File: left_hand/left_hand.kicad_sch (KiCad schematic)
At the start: 11 parts, among them M1 Motor_Servo, M2 Motor_Servo, M3 Motor_Servo, M4 Motor_Servo, M5 Motor_Servo, Q1 Q_NMOS_GDS, U1 MCP23017_SP, U2 PCA9615DP, U3 PCA9685PW

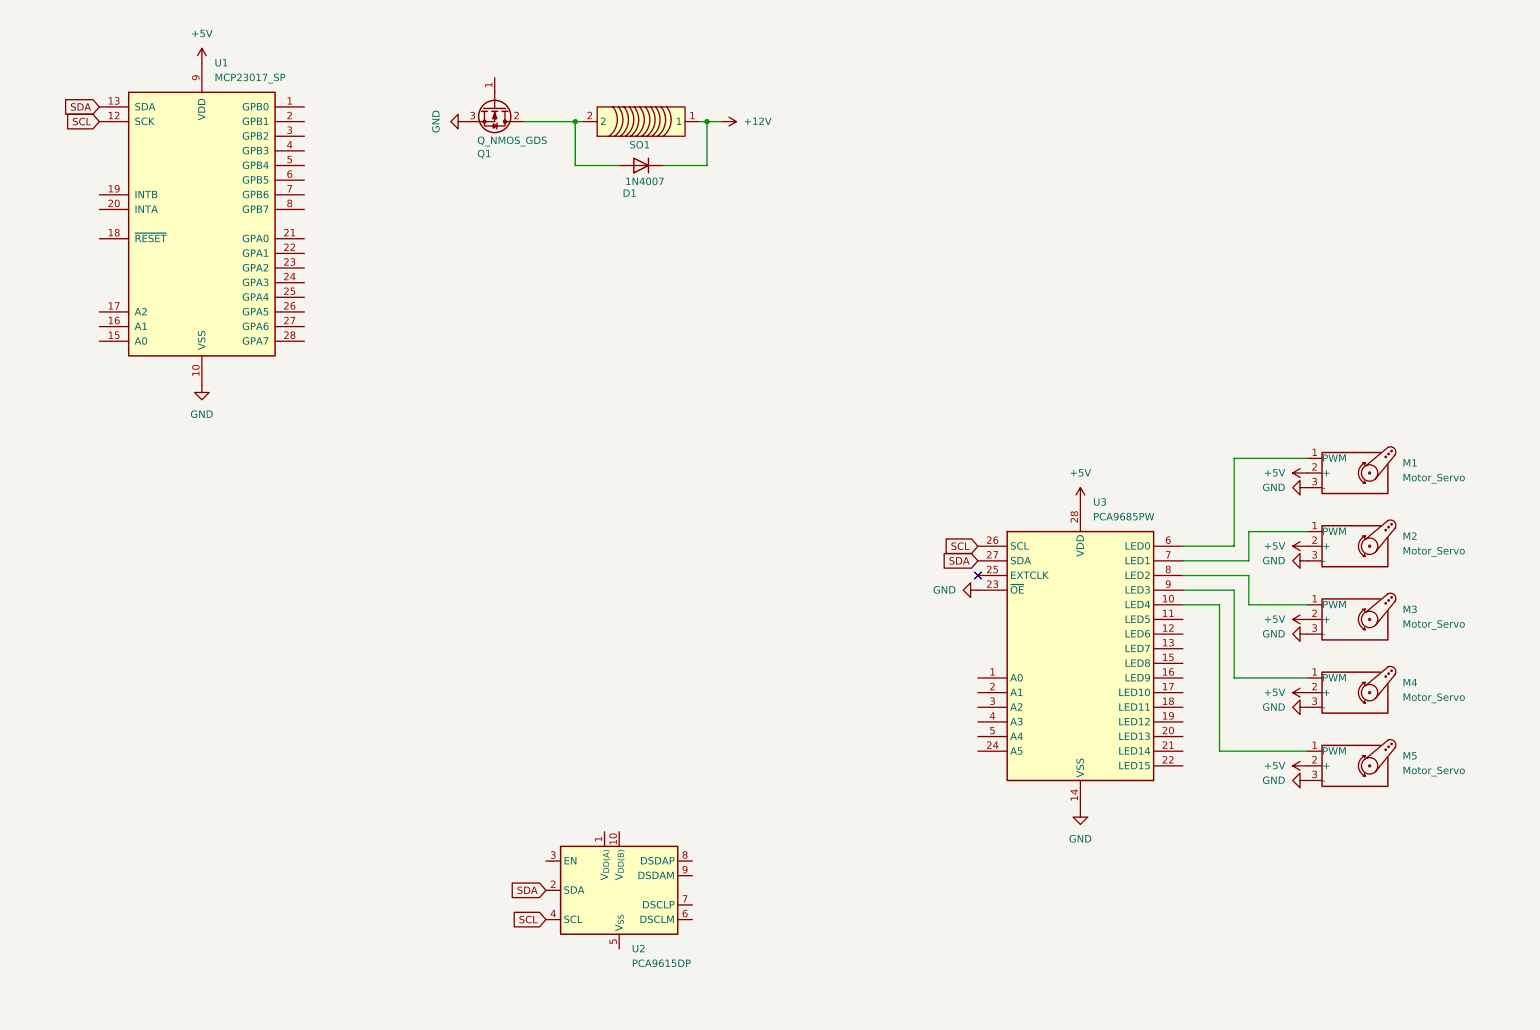
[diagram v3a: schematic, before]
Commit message: I2C diff. and single side bus changes
Added differential termination on each end. Todo: determine maximum differential bias voltage. Added pull up resistors for I2C lines.

Added decoupling caps.
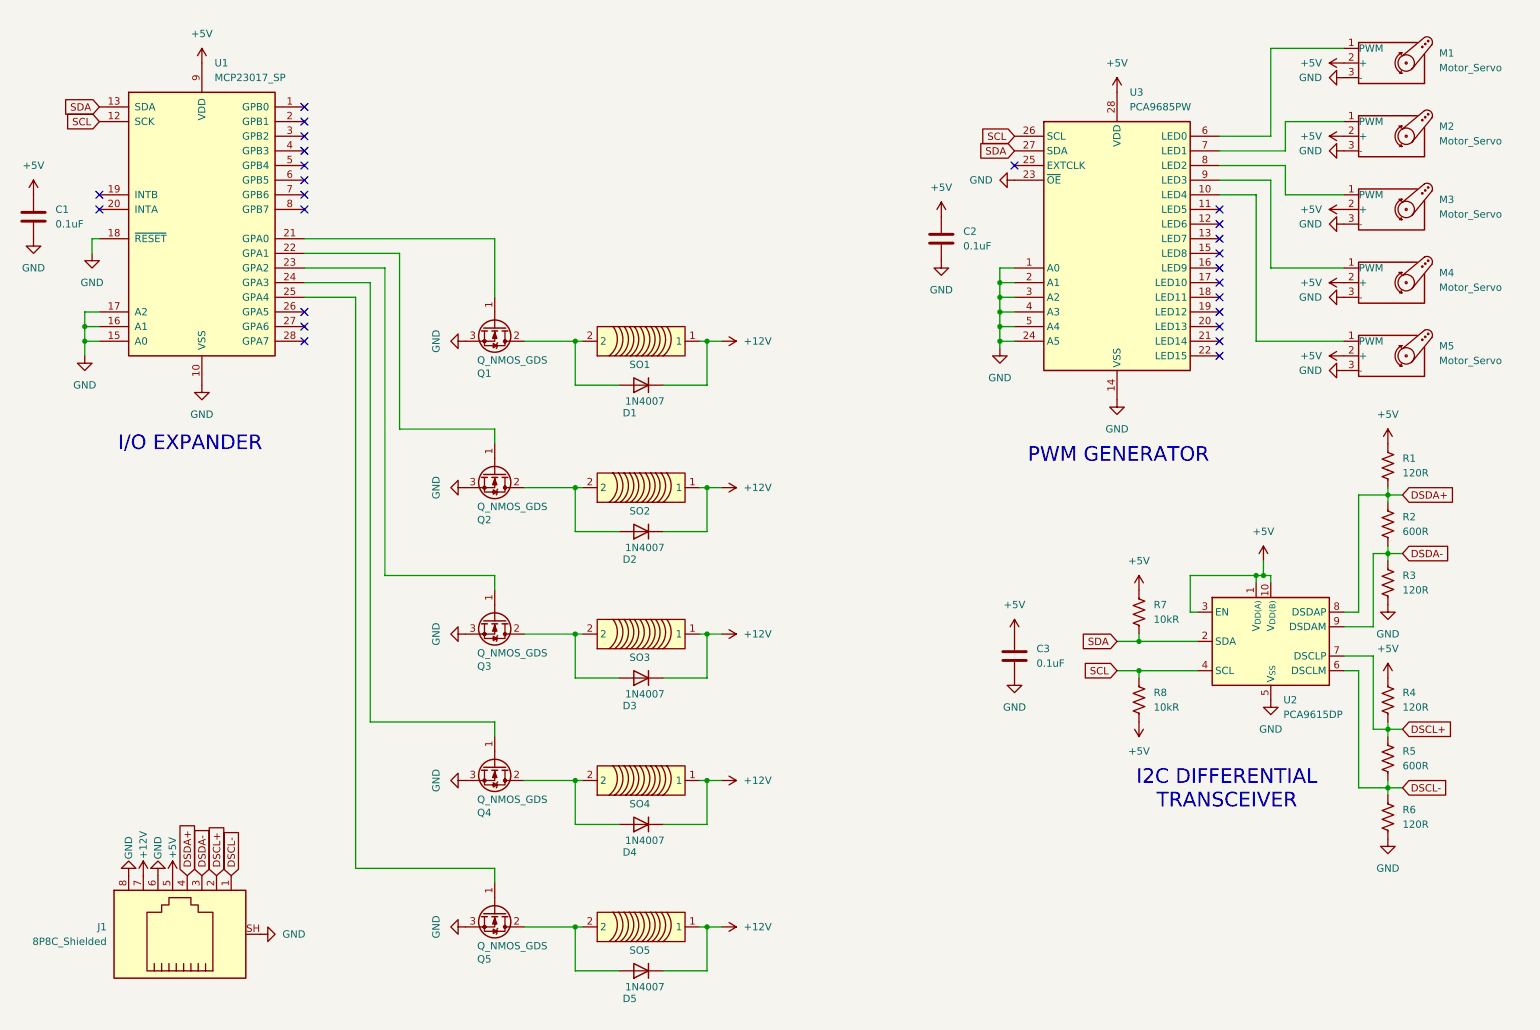
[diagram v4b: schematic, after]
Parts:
- added C1, C2, C3: 0.1uF, Capacitor_THT:C_Disc_D8.0mm_W2.5mm_P5.00mm, symbol Device:C
- added D2, D3, D4, D5: 1N4007, Diode_THT:D_DO-41_SOD81_P10.16mm_Horizontal, symbol Diode:1N4007
- added J1: 8P8C_Shielded, Connector_RJ:RJ45_Amphenol_RJHSE5380, symbol Connector:8P8C_Shielded
- added Q2, Q3, Q4, Q5: Q_NMOS_GDS, Package_TO_SOT_THT:TO-220-3_Vertical, symbol Device:Q_NMOS_GDS
- added R1, R3, R4, R6: 120R, symbol Device:R_US
- added R2, R5: 600R, symbol Device:R_US
- added R7, R8: 10kR, symbol Device:R_US
- added SO2, SO3, SO4, SO5: ~, symbol bh_symbol_library:SOLENOID
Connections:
- net +12V: now also D2.1 (K), D3.1 (K), D4.1 (K), D5.1 (K), J1.7, SO2.1, SO3.1, SO4.1, SO5.1
- net +5V: now also U2.1 (V_{DD(A)}), U2.10 (V_{DD(B)}), U2.3 (EN), C1.1, C2.1, C3.1, J1.5, R1.1, R4.1, R7.1, R8.2
- net GND: now also U1.15 (A0), U1.16 (A1), U1.17 (A2), U1.18 (~{RESET}), U2.5 (V_{SS}), U3.1 (A0), U3.2 (A1), U3.24 (A5), U3.3 (A2), U3.4 (A3), U3.5 (A4), C1.2, C2.2, C3.2, J1.6, J1.8, J1.SH, Q2.3 (S), Q3.3 (S), Q4.3 (S), Q5.3 (S), R3.2, R6.2
- net SCL: now also R8.1
- net SDA: now also R7.2
- net at U1.21 (GPA0): now also Q1.1 (G)
- net at U1.22 (GPA1): now also Q2.1 (G)
- net at U1.23 (GPA2): now also Q3.1 (G)
- net at U1.24 (GPA3): now also Q4.1 (G)
- net at U1.25 (GPA4): now also Q5.1 (G)
- net DSCL-: now reaches U2.6 (DSCLM)
- net DSCL-: now also J1.1, R5.2, R6.1
- net DSCL+: now reaches U2.7 (DSCLP)
- net DSCL+: now also J1.2, R4.2, R5.1
- net DSDA+: now reaches U2.8 (DSDAP)
- net DSDA+: now also J1.4, R1.2, R2.1
- net DSDA-: now reaches U2.9 (DSDAM)
- net DSDA-: now also J1.3, R2.2, R3.1
- new net: D4.2 (A), Q4.2 (D), SO4.2
- new net: D3.2 (A), Q3.2 (D), SO3.2
- new net: D5.2 (A), Q5.2 (D), SO5.2
- new net: D2.2 (A), Q2.2 (D), SO2.2
- no-connect marks 1 -> 25
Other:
- note added: "I/O EXPANDER"
- note added: "I2C DIFFERENTIAL TRANSCEIVER"
- note added: "PWM GENERATOR"
- moved on the sheet: D1, M1, M2, M3, M4, M5, Q1, SO1, U2, U3

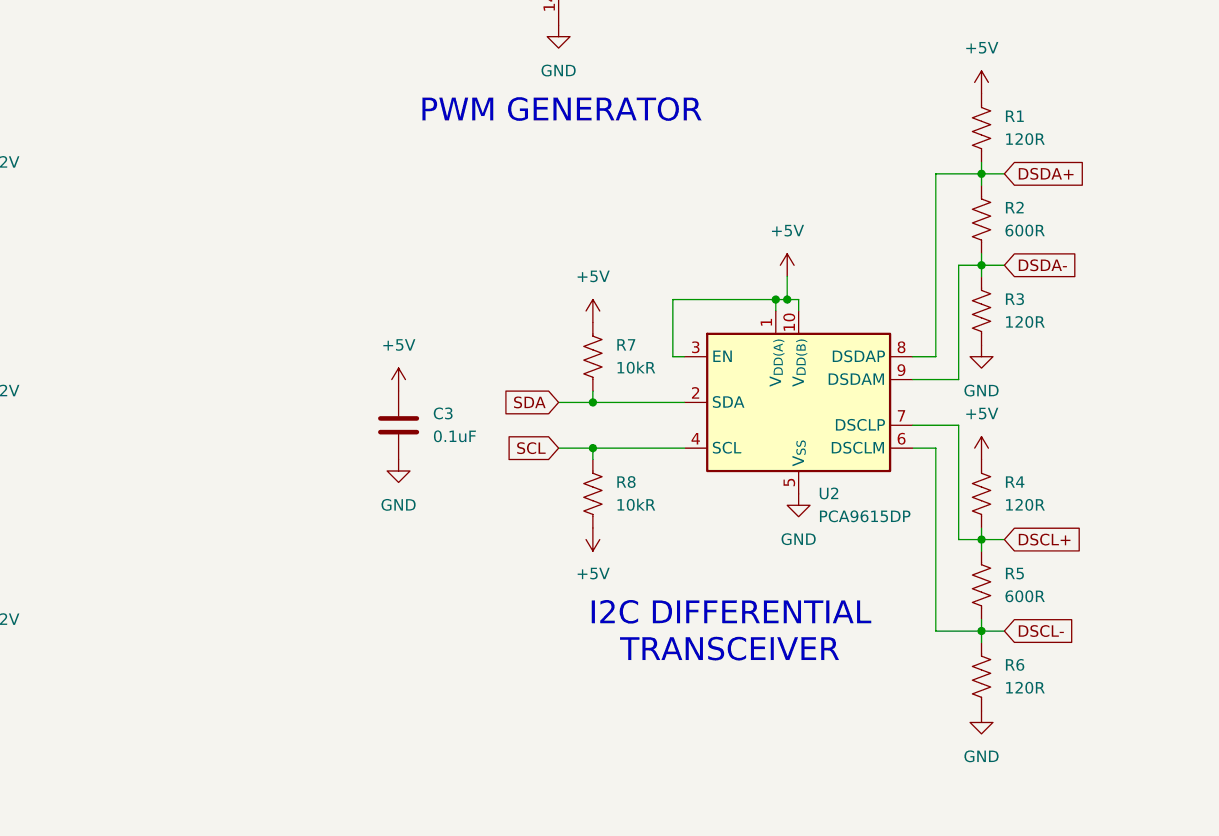
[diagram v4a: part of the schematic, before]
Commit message: Added debug headers to stuff
Added debug headers to I2C single ended lines and differential lines
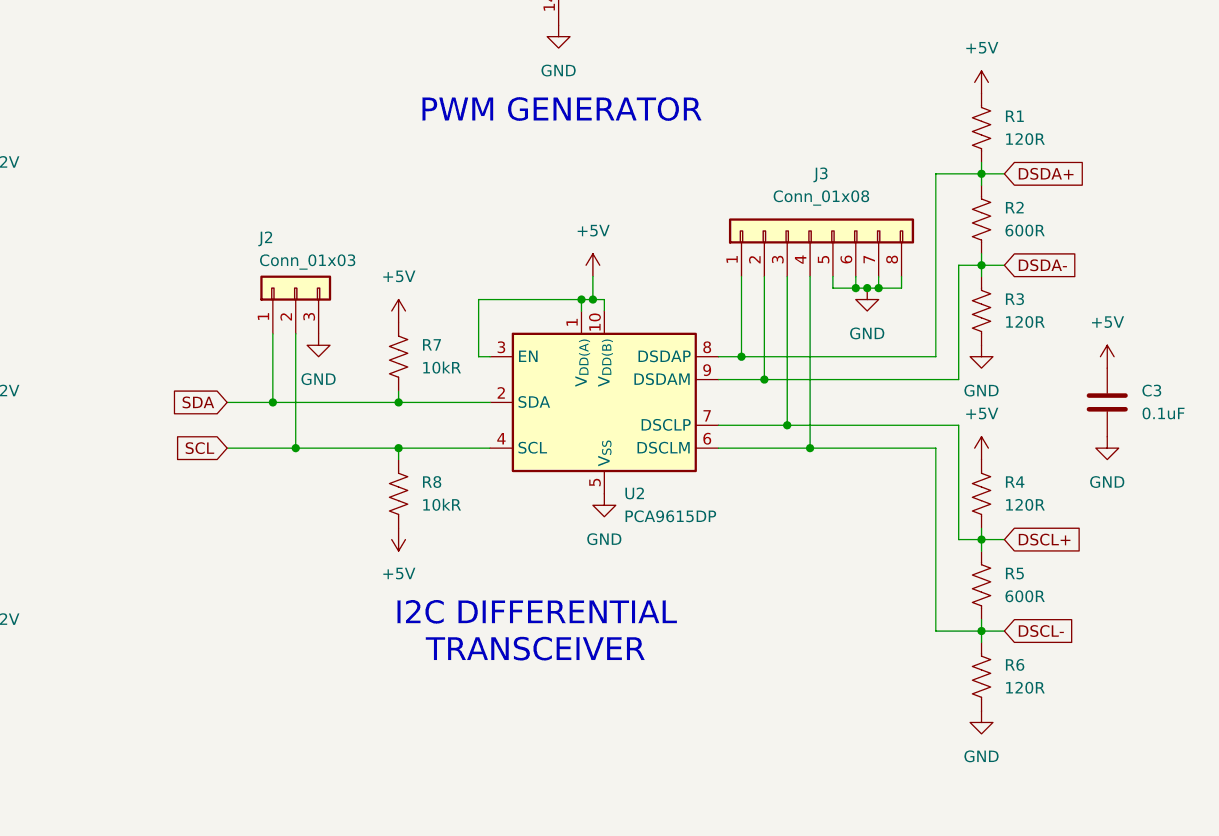
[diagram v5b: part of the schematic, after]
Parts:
- added J2: Conn_01x03, Connector_PinHeader_2.54mm:PinHeader_1x03_P2.54mm_Vertical, symbol Connector_Generic:Conn_01x03
- added J3: Conn_01x08, Connector_PinHeader_2.54mm:PinHeader_1x08_P2.54mm_Vertical, symbol Connector_Generic:Conn_01x08
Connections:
- net DSCL+: now also J3.3 (Pin_3)
- net DSCL-: now also J3.4 (Pin_4)
- net DSDA+: now also J3.1 (Pin_1)
- net DSDA-: now also J3.2 (Pin_2)
- net GND: now also J2.3 (Pin_3), J3.5 (Pin_5), J3.6 (Pin_6), J3.7 (Pin_7), J3.8 (Pin_8)
- net SCL: now also J2.2 (Pin_2)
- net SDA: now also J2.1 (Pin_1)
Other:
- moved on the sheet: C3, R7, R8, U2

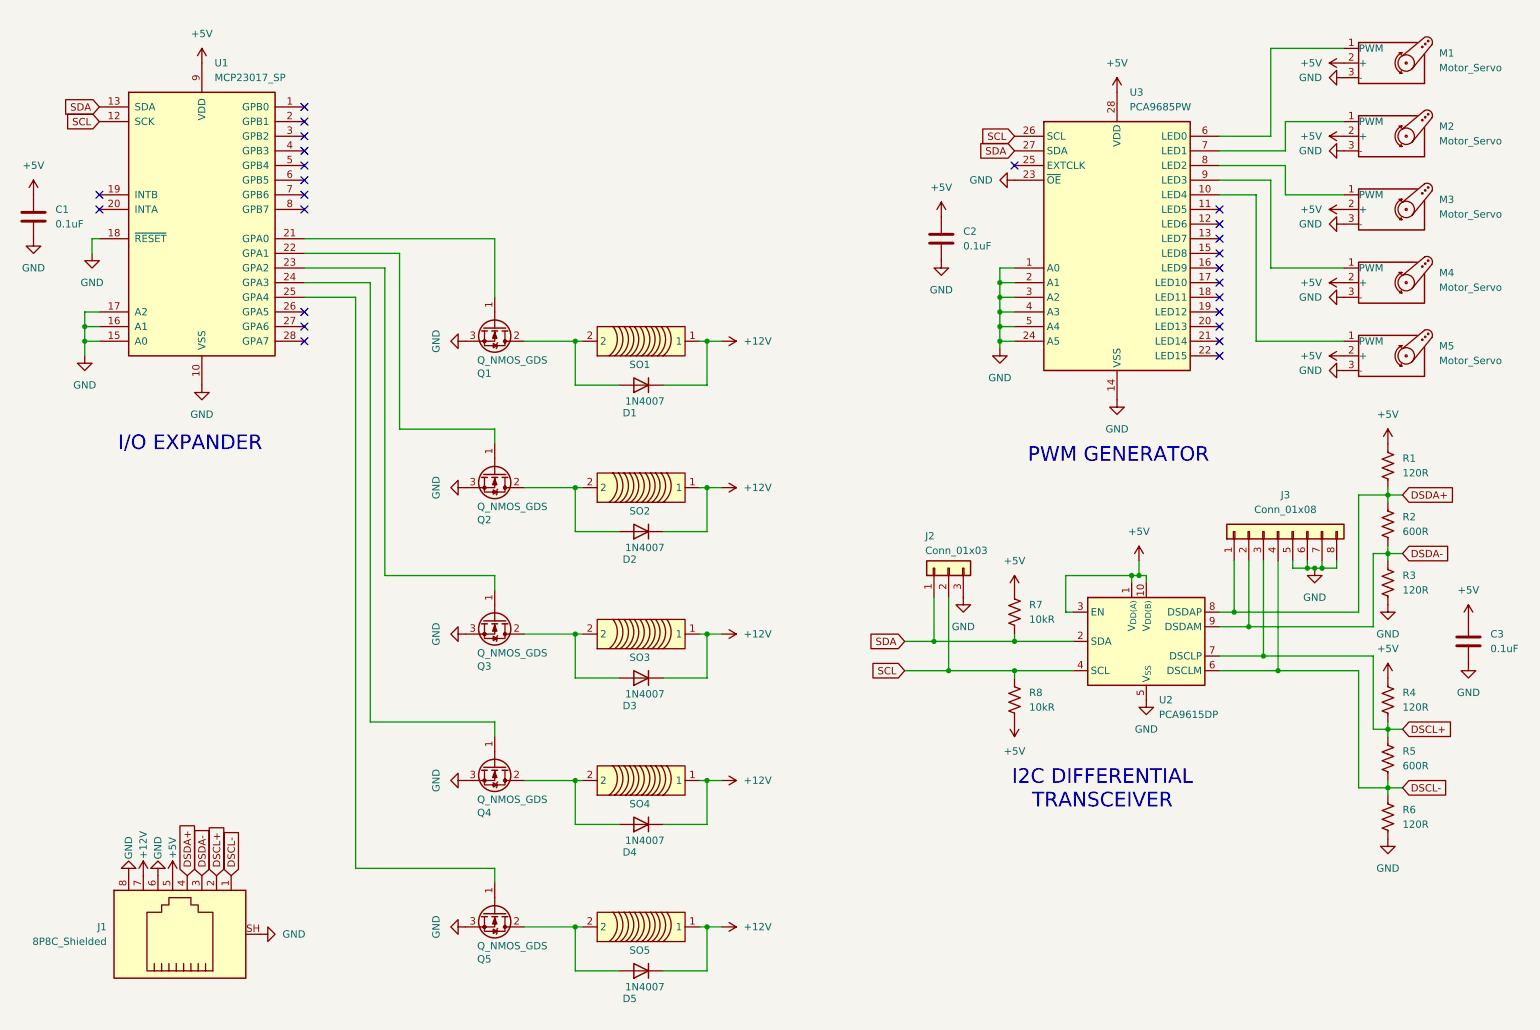
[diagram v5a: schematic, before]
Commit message: Added ICs
Added ADC IC
Switched to schottky flyback diode for better response times
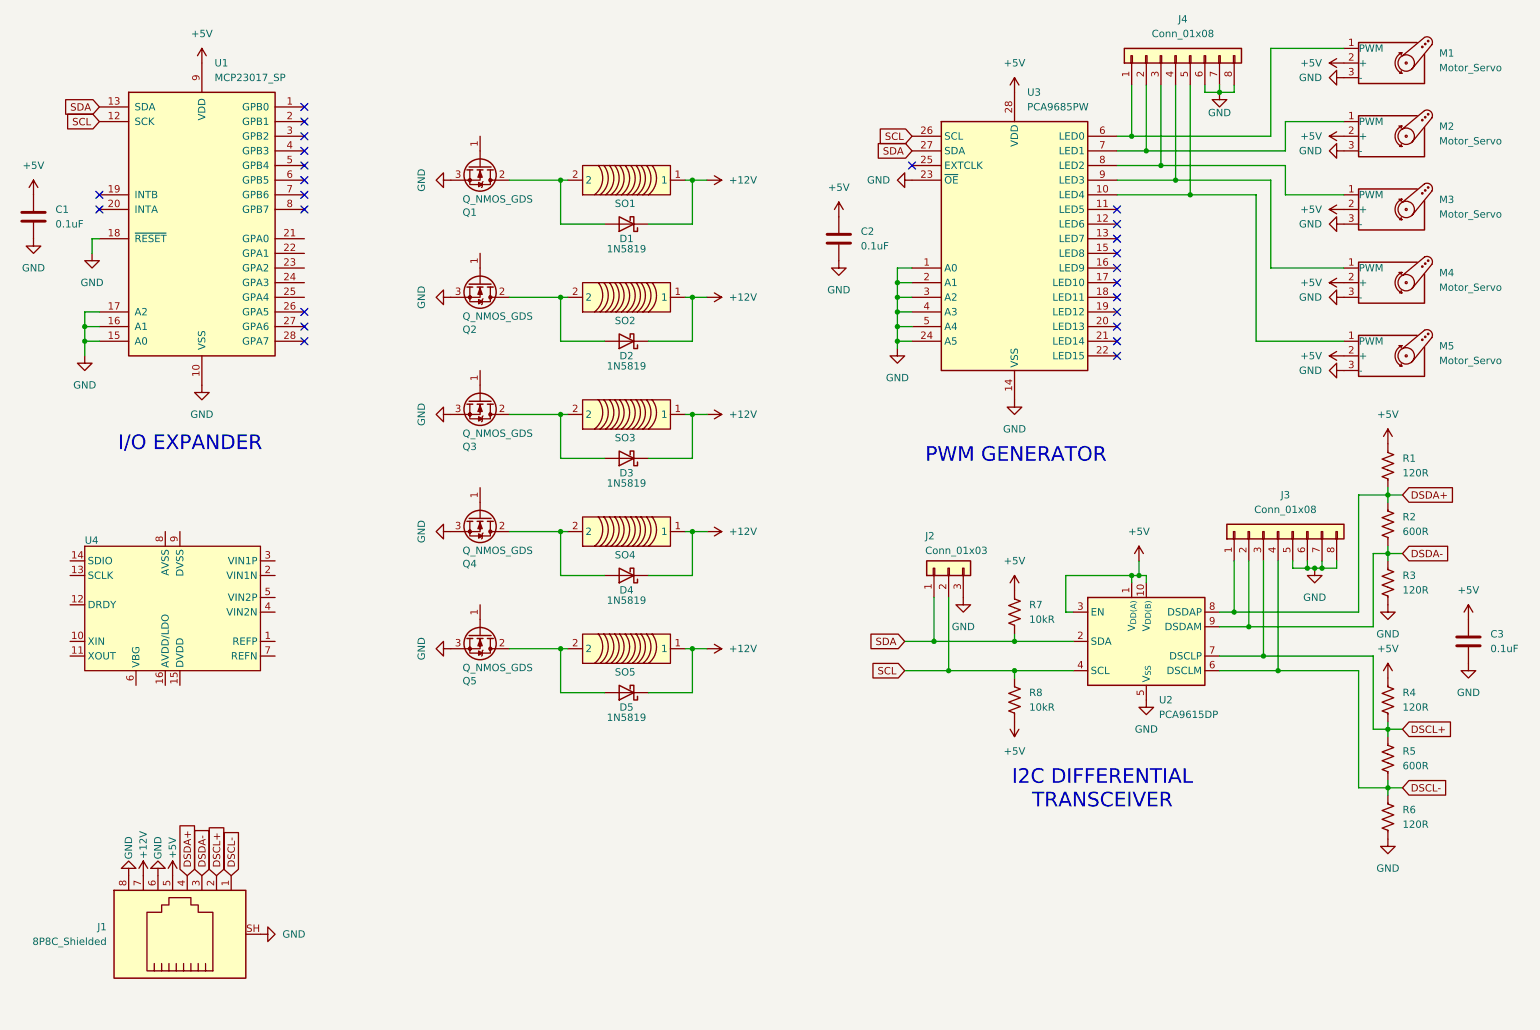
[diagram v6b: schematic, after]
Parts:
- removed D1, D2, D3, D4, D5: 1N4007, Diode_THT:D_DO-41_SOD81_P10.16mm_Horizontal, symbol Diode:1N4007
- added D1, D2, D3, D4, D5: 1N5819, Diode_THT:D_DO-41_SOD81_P10.16mm_Horizontal, symbol Diode:1N5819
- added J4: Conn_01x08, Connector_PinHeader_2.54mm:PinHeader_1x08_P2.54mm_Vertical, symbol Connector_Generic:Conn_01x08
- added U4: ~, symbol bh_symbol_library:NAU7802KGI
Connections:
- net +12V: now also D1.1 (K), D2.1 (K), D3.1 (K), D4.1 (K), D5.1 (K)
- net GND: now also J4.6 (Pin_6), J4.7 (Pin_7), J4.8 (Pin_8)
- net at Q4.2 (D), SO4.2: now also D4.2 (A)
- net at Q4.1 (G): no longer U1.24 (GPA3)
- net at Q3.1 (G): no longer U1.23 (GPA2)
- net at Q3.2 (D), SO3.2: now also D3.2 (A)
- net at U1.21 (GPA0): no longer Q1.1 (G)
- net at U1.22 (GPA1): no longer Q2.1 (G)
- net at U1.25 (GPA4): no longer Q5.1 (G)
- net at M3.1 (PWM), U3.8 (LED2): now also J4.3 (Pin_3)
- net at M5.1 (PWM), U3.10 (LED4): now also J4.5 (Pin_5)
- net at M1.1 (PWM), U3.6 (LED0): now also J4.1 (Pin_1)
- net at M2.1 (PWM), U3.7 (LED1): now also J4.2 (Pin_2)
- net at M4.1 (PWM), U3.9 (LED3): now also J4.4 (Pin_4)
- net at Q5.2 (D), SO5.2: now also D5.2 (A)
- net at Q1.2 (D), SO1.2: now also D1.2 (A)
- net at Q2.2 (D), SO2.2: now also D2.2 (A)
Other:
- moved on the sheet: C2, Q1, Q2, Q3, Q4, Q5, SO1, SO2, SO3, SO4, SO5, U3
